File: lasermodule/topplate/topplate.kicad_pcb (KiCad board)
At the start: 2 copper layers, 89 x 60 mm, 3 parts

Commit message: simplified loading in freecad, updated pcbs
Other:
- board text added: "PCB3D_BR_topplate"
- board text added: "PCB3D_TL_topplate"

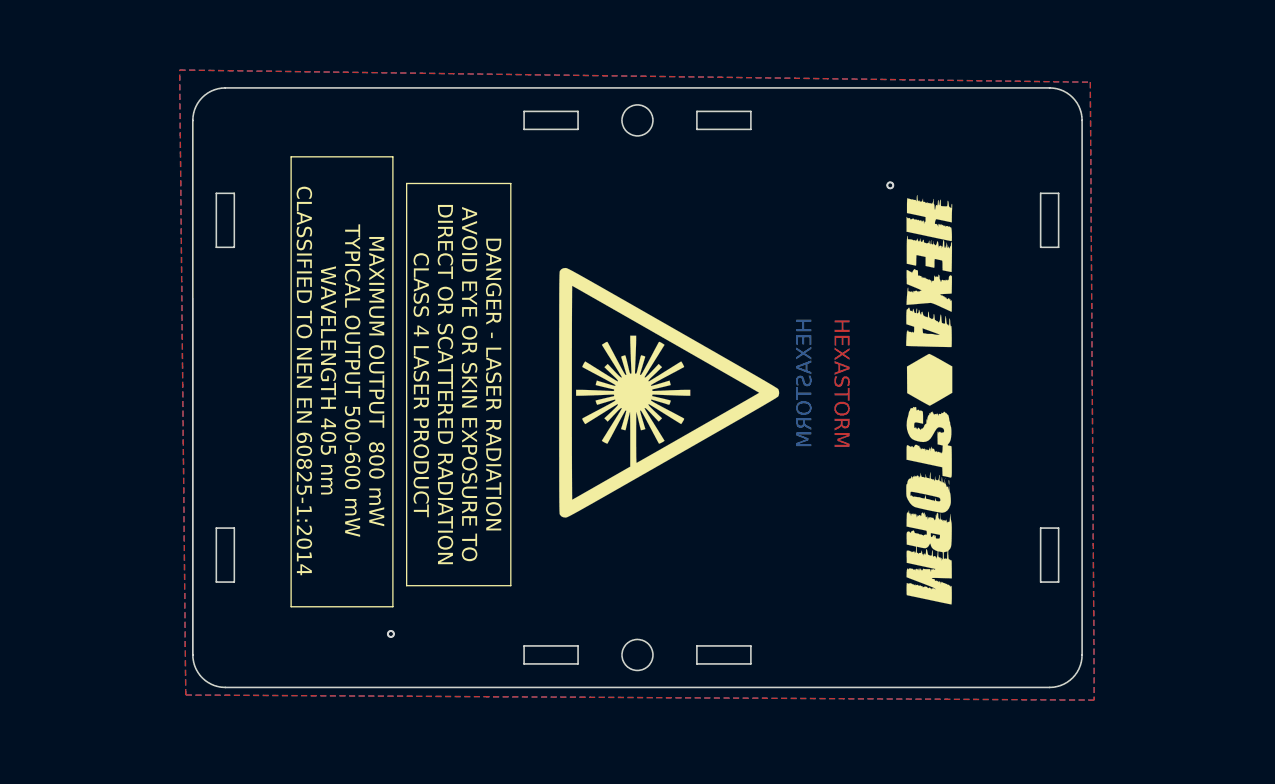
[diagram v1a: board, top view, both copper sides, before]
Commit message: pcbs can be rendered
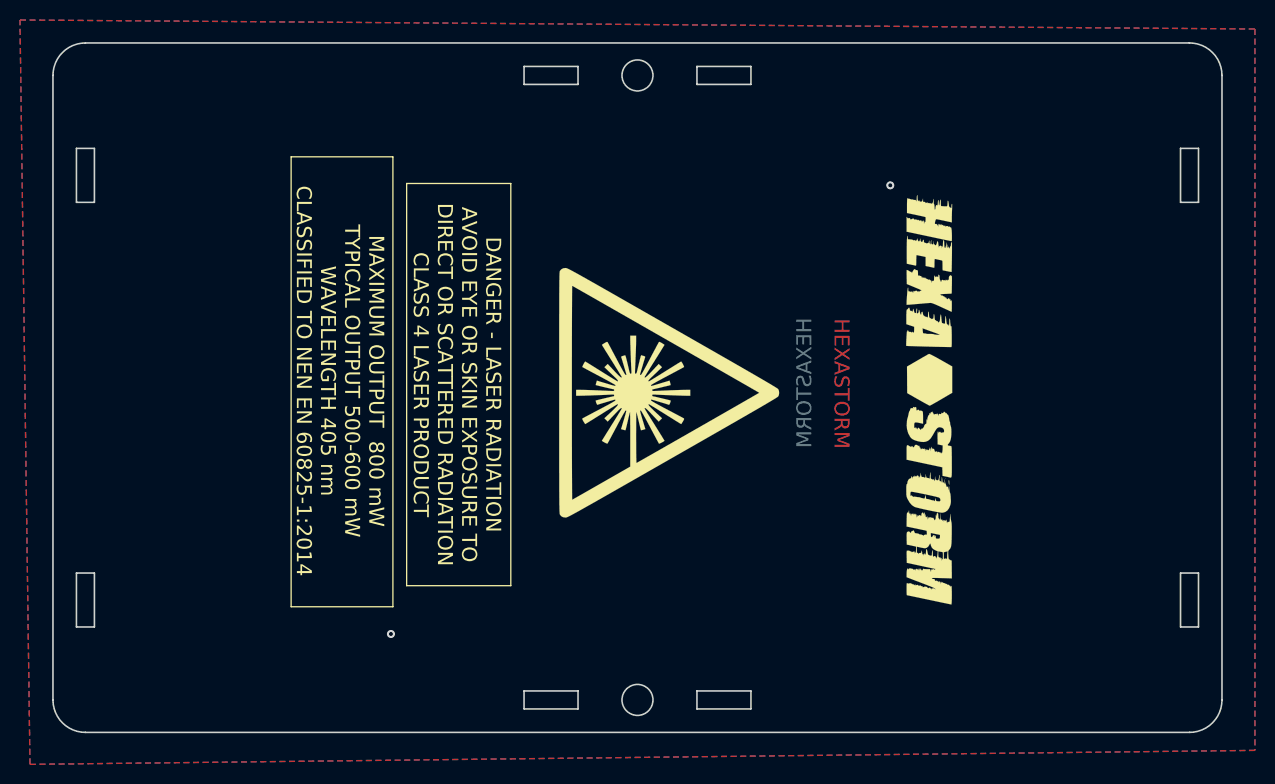
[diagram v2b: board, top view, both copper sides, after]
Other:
- board size 89 x 60 mm -> 117 x 69 mm
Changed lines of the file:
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@@
   (gr_line (start 141.43736 123.76912) (end 141.43736 83.51266)
     (stroke (width 0.12) (type solid)) (layer "F.SilkS"))
-  (gr_line (start 148.165 131.6) (end 142.764 131.6)
+  (gr_line (start 208.4645 85.3995) (end 208.4645 79.9995)
     (stroke (width 0.16) (type solid)) (layer "Edge.Cuts"))
-  (gr_line (start 109.614 77.2) (end 109.615 130.7)
+  (gr_line (start 208.4645 127.8995) (end 208.4645 122.4995)
     (stroke (width 0.16) (type solid)) (layer "Edge.Cuts"))
-  (gr_line (start 194.464 89.899) (end 194.464 84.499)
+  (gr_line (start 160.0645 134.2995) (end 165.4645 134.2995)
     (stroke (width 0.16) (type solid)) (layer "Edge.Cuts"))
-  (gr_arc (start 195.364 73.95) (mid 197.663 74.901) (end 198.614 77.2)
+  (gr_line (start 210.2645 127.8995) (end 208.4645 127.8995)
     (stroke (width 0.16) (type solid)) (layer "Edge.Cuts"))
-  (gr_line (start 194.464 84.499) (end 196.264 84.499)
+  (gr_circle (center 154.1145 72.6995) (end 152.5645 72.6995)
+    (stroke (width 0.16) (type solid)) (fill none) (layer "Edge.Cuts"))
+  (gr_line (start 148.1645 136.0995) (end 142.7645 136.0995)
     (stroke (width 0.16) (type solid)) (layer "Edge.Cuts"))
-  (gr_line (start 112.864 133.95) (end 195.364 133.95)
+  (gr_line (start 148.1645 71.7995) (end 148.1645 73.5995)
     (stroke (width 0.16) (type solid)) (layer "Edge.Cuts"))
-  (gr_circle (center 154.114 77.2) (end 152.564 77.2)
+  (gr_line (start 99.7645 122.4995) (end 99.7645 127.8995)
+    (stroke (width 0.16) (type solid)) (layer "Edge.Cuts"))
+  (gr_line (start 99.7645 79.9995) (end 99.7645 85.3995)
+    (stroke (width 0.16) (type solid)) (layer "Edge.Cuts"))
+  (gr_line (start 97.9645 127.8995) (end 97.9645 122.4995)
+    (stroke (width 0.16) (type solid)) (layer "Edge.Cuts"))
+  (gr_arc (start 209.3645 69.4495) (mid 211.662597 70.401403) (end 212.6145 72.6995)
+    (stroke (width 0.16) (type solid)) (layer "Edge.Cuts"))
+  (gr_line (start 99.7645 127.8995) (end 97.9645 127.8995)
+    (stroke (width 0.16) (type solid)) (layer "Edge.Cuts"))
+  (gr_line (start 165.4645 73.5995) (end 160.0645 73.5995)
+    (stroke (width 0.16) (type solid)) (layer "Edge.Cuts"))
+  (gr_line (start 160.0645 136.0995) (end 160.0645 134.2995)
+    (stroke (width 0.16) (type solid)) (layer "Edge.Cuts"))
+  (gr_line (start 99.7645 85.3995) (end 97.9645 85.3995)
+    (stroke (width 0.16) (type solid)) (layer "Edge.Cuts"))
+  (gr_line (start 165.4645 136.0995) (end 160.0645 136.0995)
+    (stroke (width 0.16) (type solid)) (layer "Edge.Cuts"))
+  (gr_line (start 208.4645 79.9995) (end 210.2645 79.9995)
+    (stroke (width 0.16) (type solid)) (layer "Edge.Cuts"))
+  (gr_line (start 160.0645 71.7995) (end 165.4645 71.7995)
+    (stroke (width 0.16) (type solid)) (layer "Edge.Cuts"))
+  (gr_circle (center 154.1145 135.1995) (end 152.5645 135.1995)
     (stroke (width 0.16) (type solid)) (fill none) (layer "Edge.Cuts"))
-  (gr_line (start 194.464 117.999) (end 196.264 117.999)
+  (gr_line (start 210.2645 85.3995) (end 208.4645 85.3995)
     (stroke (width 0.16) (type solid)) (layer "Edge.Cuts"))
-  (gr_line (start 196.264 117.999) (end 196.264 123.4)
+  (gr_line (start 142.7645 134.2995) (end 148.1645 134.2995)
     (stroke (width 0.16) (type solid)) (layer "Edge.Cuts"))
-  (gr_line (start 111.964 84.499) (end 113.764 84.499)
+  (gr_line (start 212.6145 72.6995) (end 212.6145 135.1995)
     (stroke (width 0.16) (type solid)) (layer "Edge.Cuts"))
-  (gr_line (start 165.464 78.1) (end 160.064 78.1)
+  (gr_line (start 98.8645 138.4495) (end 209.3645 138.4495)
     (stroke (width 0.16) (type solid)) (layer "Edge.Cuts"))
-  (gr_arc (start 109.614 77.2) (mid 110.566 74.901) (end 112.864 73.95)
+  (gr_line (start 95.6145 72.6995) (end 95.6145 135.1995)
     (stroke (width 0.16) (type solid)) (layer "Edge.Cuts"))
-  (gr_line (start 111.965 118) (end 113.765 118)
+  (gr_line (start 97.9645 85.3995) (end 97.9645 79.9995)
     (stroke (width 0.16) (type solid)) (layer "Edge.Cuts"))
-  (gr_line (start 160.064 78.1) (end 160.064 76.299)
+  (gr_line (start 142.7645 136.0995) (end 142.7645 134.2995)
     (stroke (width 0.16) (type solid)) (layer "Edge.Cuts"))
-  (gr_line (start 160.064 76.299) (end 165.464 76.299)
+  (gr_line (start 98.8645 69.4495) (end 209.3645 69.4495)
     (stroke (width 0.16) (type solid)) (layer "Edge.Cuts"))
-  (gr_line (start 165.464 129.799) (end 165.464 131.6)
+  (gr_line (start 210.2645 79.9995) (end 210.2645 85.3995)
     (stroke (width 0.16) (type solid)) (layer "Edge.Cuts"))
-  (gr_line (start 142.764 129.799) (end 148.165 129.799)
+  (gr_line (start 210.2645 122.4995) (end 210.2645 127.8995)
     (stroke (width 0.16) (type solid)) (layer "Edge.Cuts"))
-  (gr_line (start 113.765 123.4) (end 111.965 123.4)
+  (gr_line (start 208.4645 122.4995) (end 210.2645 122.4995)
     (stroke (width 0.16) (type solid)) (layer "Edge.Cuts"))
-  (gr_line (start 198.614 77.2) (end 198.614 130.7)
+  (gr_line (start 160.0645 73.5995) (end 160.0645 71.7995)
     (stroke (width 0.16) (type solid)) (layer "Edge.Cuts"))
-  (gr_line (start 194.464 123.4) (end 194.464 117.999)
+  (gr_line (start 142.7645 73.5995) (end 142.7645 71.7995)
     (stroke (width 0.16) (type solid)) (layer "Edge.Cuts"))
-  (gr_line (start 148.165 78.1) (end 142.764 78.1)
+  (gr_line (start 165.4645 134.2995) (end 165.4645 136.0995)
     (stroke (width 0.16) (type solid)) (layer "Edge.Cuts"))
-  (gr_line (start 142.764 76.299) (end 148.165 76.299)
+  (gr_line (start 165.4645 71.7995) (end 165.4645 73.5995)
     (stroke (width 0.16) (type solid)) (layer "Edge.Cuts"))
-  (gr_line (start 165.464 131.6) (end 160.064 131.6)
+  (gr_arc (start 212.6145 135.1995) (mid 211.662597 137.497597) (end 209.3645 138.4495)
     (stroke (width 0.16) (type solid)) (layer "Edge.Cuts"))
-  (gr_line (start 148.165 76.299) (end 148.165 78.1)
+  (gr_line (start 148.1645 134.2995) (end 148.1645 136.0995)
     (stroke (width 0.16) (type solid)) (layer "Edge.Cuts"))
-  (gr_line (start 112.864 73.95) (end 195.364 73.95)
+  (gr_arc (start 98.8645 138.4495) (mid 96.566403 137.497597) (end 95.6145 135.1995)
     (stroke (width 0.16) (type solid)) (layer "Edge.Cuts"))
-  (gr_line (start 113.764 89.899) (end 111.964 89.899)
+  (gr_line (start 142.7645 71.7995) (end 148.1645 71.7995)
     (stroke (width 0.16) (type solid)) (layer "Edge.Cuts"))
-  (gr_line (start 111.965 123.4) (end 111.965 118)
+  (gr_line (start 97.9645 122.4995) (end 99.7645 122.4995)
     (stroke (width 0.16) (type solid)) (layer "Edge.Cuts"))
-  (gr_line (start 160.064 129.799) (end 165.464 129.799)
+  (gr_line (start 148.1645 73.5995) (end 142.7645 73.5995)
     (stroke (width 0.16) (type solid)) (layer "Edge.Cuts"))
-  (gr_line (start 113.764 84.499) (end 113.764 89.899)
+  (gr_line (start 97.9645 79.9995) (end 99.7645 79.9995)
     (stroke (width 0.16) (type solid)) (layer "Edge.Cuts"))
-  (gr_line (start 142.764 131.6) (end 142.764 129.799)
-    (stroke (width 0.16) (type solid)) (layer "Edge.Cuts"))
-  (gr_line (start 165.464 76.299) (end 165.464 78.1)
-    (stroke (width 0.16) (type solid)) (layer "Edge.Cuts"))
-  (gr_line (start 111.964 89.899) (end 111.964 84.499)
-    (stroke (width 0.16) (type solid)) (layer "Edge.Cuts"))
-  (gr_line (start 113.765 118) (end 113.765 123.4)
-    (stroke (width 0.16) (type solid)) (layer "Edge.Cuts"))
-  (gr_arc (start 112.864 133.95) (mid 110.566 132.998) (end 109.615 130.7)
-    (stroke (width 0.16) (type solid)) (layer "Edge.Cuts"))
-  (gr_line (start 160.064 131.6) (end 160.064 129.799)
-    (stroke (width 0.16) (type solid)) (layer "Edge.Cuts"))
-  (gr_circle (center 154.114 130.7) (end 152.564 130.7)
-    (stroke (width 0.16) (type solid)) (fill none) (layer "Edge.Cuts"))
-  (gr_line (start 142.764 78.1) (end 142.764 76.299)
-    (stroke (width 0.16) (type solid)) (layer "Edge.Cuts"))
-  (gr_line (start 196.264 89.899) (end 194.464 89.899)
-    (stroke (width 0.16) (type solid)) (layer "Edge.Cuts"))
-  (gr_line (start 196.264 84.499) (end 196.264 89.899)
-    (stroke (width 0.16) (type solid)) (layer "Edge.Cuts"))
-  (gr_line (start 148.165 129.799) (end 148.165 131.6)
-    (stroke (width 0.16) (type solid)) (layer "Edge.Cuts"))
-  (gr_line (start 196.264 123.4) (end 194.464 123.4)
-    (stroke (width 0.16) (type solid)) (layer "Edge.Cuts"))
-  (gr_arc (start 198.614 130.7) (mid 197.663 132.998) (end 195.364 133.95)
+  (gr_arc (start 95.6145 72.6995) (mid 96.566403 70.401403) (end 98.8645 69.4495)
     (stroke (width 0.16) (type solid)) (layer "Edge.Cuts"))
   (gr_text "HEXASTORM" (at 174.5345 103.5395 270) (layer "F.Cu")
@@
     (effects (font (size 1 1) (thickness 0.15)))
   )
-  (gr_text "PCB3D_BR_topplate" (at 176.9745 136.9695) (layer "Cmts.User")
+  (gr_text "PCB3D_BR_topplate" (at 214.6145 143.3495) (layer "Cmts.User")
     (effects (font (size 1.5 1.5) (thickness 0.3) bold) (justify left bottom))
   )
-  (gr_text "PCB3D_TL_topplate" (at 108.3945 70.9295) (layer "Cmts.User")
+  (gr_text "PCB3D_TL_topplate" (at 94.4145 65.7495) (layer "Cmts.User")
     (effects (font (size 1.5 1.5) (thickness 0.3) bold) (justify left bottom))
   )
@@
     (polygon
       (pts
-        (xy 199.8345 135.2195)
-        (xy 108.9045 134.7095)
-        (xy 108.2945 72.1595)
-        (xy 199.4345 73.3795)
+        (xy 215.9145 140.2495)
+        (xy 93.3145 141.6495)
+        (xy 92.3145 67.1495)
+        (xy 215.9145 68.0495)
       )
     )

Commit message: changed position logos
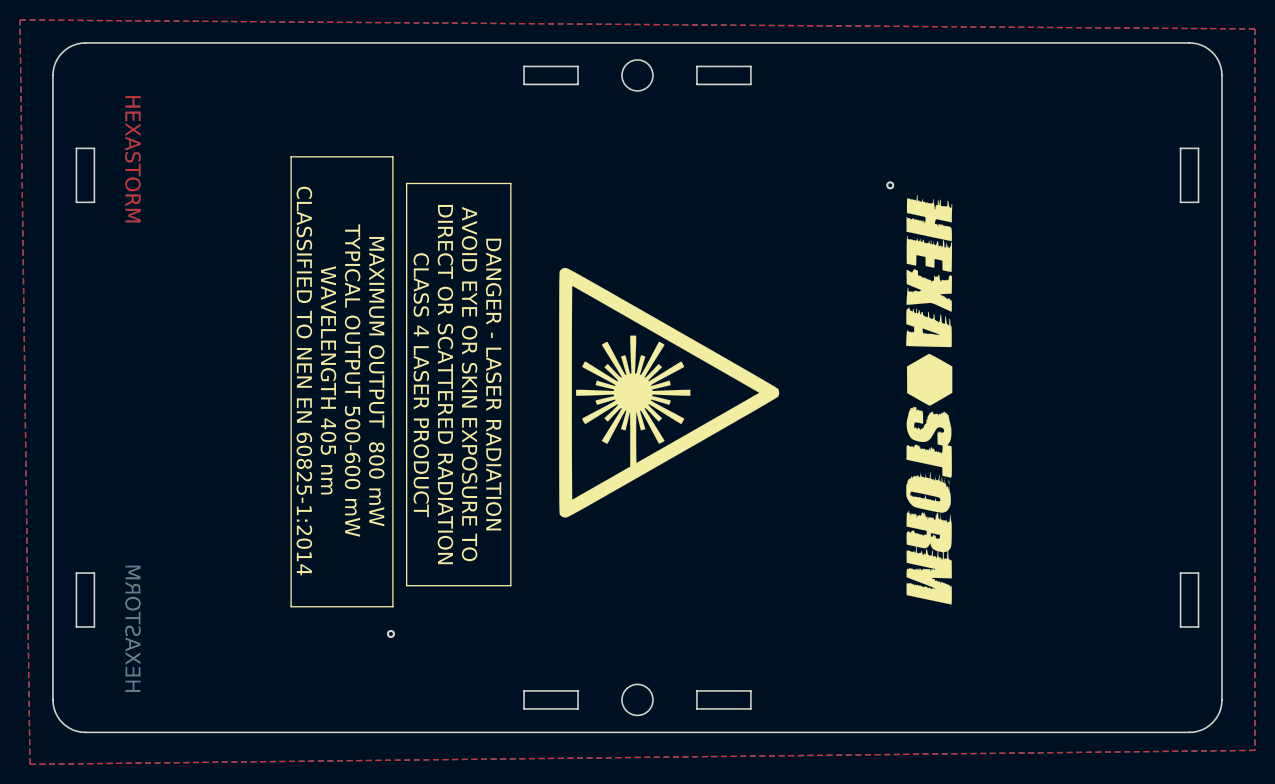
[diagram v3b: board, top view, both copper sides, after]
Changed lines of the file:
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@@
   (gr_arc (start 95.6145 72.6995) (mid 96.566403 70.401403) (end 98.8645 69.4495)
     (stroke (width 0.16) (type solid)) (layer "Edge.Cuts"))
-  (gr_text "HEXASTORM" (at 174.5345 103.5395 270) (layer "F.Cu")
+  (gr_text "HEXASTORM" (at 103.5685 81.0895 270) (layer "F.Cu")
     (effects (font (size 1.5 1.5) (thickness 0.3)))
   )
-  (gr_text "HEXASTORM" (at 170.8145 103.4745 90) (layer "B.Cu")
+  (gr_text "HEXASTORM" (at 103.5685 128.0795 270) (layer "B.Cu")
     (effects (font (size 1.5 1.5) (thickness 0.3)) (justify mirror))
   )
@@
     (effects (font (size 1.5 1.5) (thickness 0.3)))
   )
-  (gr_text "HEXASTORM" (at 172.9395 114.0995 90) (layer "B.Mask")
+  (gr_text "HEXASTORM" (at 103.5685 80.5815 270) (layer "B.Mask")
     (effects (font (size 1 1) (thickness 0.15)) (justify mirror))
   )
-  (gr_text "HEXASTORM" (at 172.7395 91.9245 90) (layer "F.Mask")
+  (gr_text "HEXASTORM" (at 103.5685 129.0955 270) (layer "F.Mask")
     (effects (font (size 1 1) (thickness 0.15)))
   )
